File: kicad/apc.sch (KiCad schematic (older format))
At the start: 13 parts, among them U101 LM556

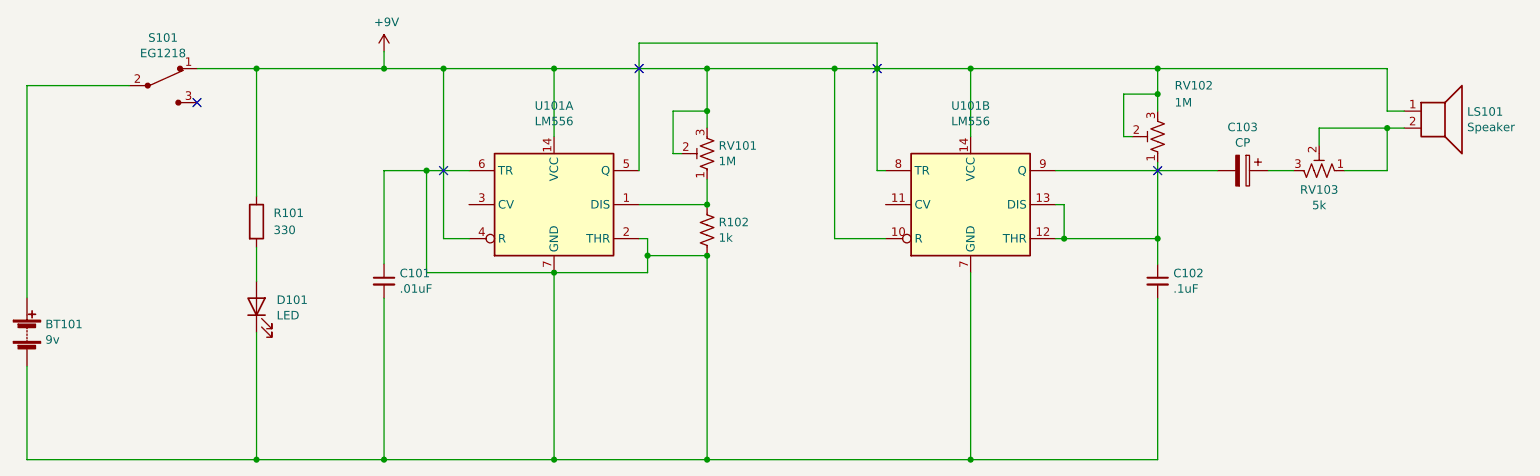
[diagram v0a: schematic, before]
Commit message: PCB revisions:
* Fix APC ground error
* Add voltage regulator to POLY_555
* Ditch hitch
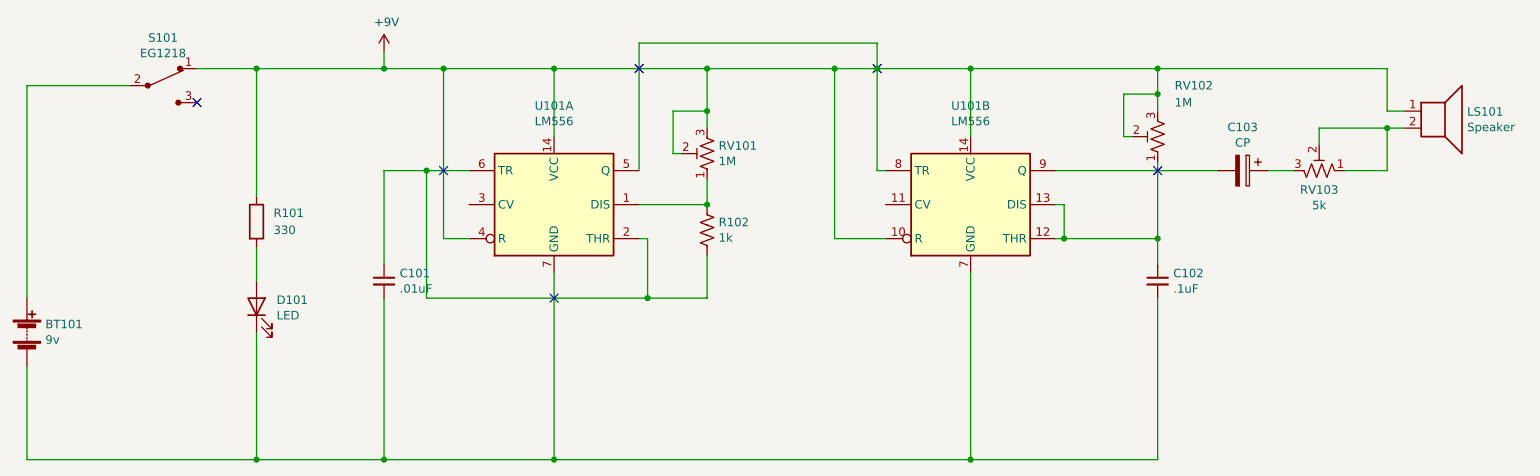
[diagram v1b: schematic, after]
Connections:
- net at BT101.2 (-), C101.2, C102.2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: no longer C101.1, R102.2, U101.2 (THR), U101.6 (TR)
- new net: C101.1, R102.2, U101.2 (THR), U101.6 (TR)
- no-connect marks 5 -> 6
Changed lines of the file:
@@
 	-1   0    0    1
-$EndComp
-$Comp
-L Timer:LM556 U101
-U 1 1 5F4726A4
-P 4150 3500
-F 0 "U101" H 4150 4081 50  0000 C CNN
-F 1 "LM556" H 4150 3990 50  0000 C CNN
-F 2 "Package_DIP:DIP-14_W7.62mm_LongPads" H 4150 3500 50  0001 C CNN
-F 3 "http://www.ti.com/lit/ds/symlink/lm556.pdf" H 4150 3500 50  0001 C CNN
-	1    4150 3500
-	1    0    0    -1
 $EndComp
 Wire Wire Line
@@
 Wire Wire Line
 	4650 3700 4700 3700
-Wire Wire Line
-	4700 3700 4700 3800
-Wire Wire Line
-	4700 3800 5050 3800
-Wire Wire Line
-	3650 3300 3400 3300
-Wire Wire Line
-	5050 5000 5050 3800
-Connection ~ 5050 3800
-Wire Wire Line
-	5050 5000 6600 5000
-Connection ~ 5050 5000
 Wire Wire Line
 	4650 3300 4650 2550
@@
 Wire Wire Line
 	3150 5000 4150 5000
-Wire Wire Line
-	4150 3900 4150 5000
 Connection ~ 4150 5000
-Wire Wire Line
-	4150 5000 5050 5000
 Wire Wire Line
 	6600 3900 6600 5000
 Connection ~ 6600 5000
-Wire Wire Line
-	3400 3300 3400 3900
-Wire Wire Line
-	3400 3900 4150 3900
-Wire Wire Line
-	4700 3900 4700 3800
-Connection ~ 3400 3300
-Wire Wire Line
-	3400 3300 3150 3300
-Connection ~ 4150 3900
-Wire Wire Line
-	4150 3900 4700 3900
-Connection ~ 4700 3800
 $Comp
 L Timer:LM556 U101
@@
 Wire Wire Line
 	6600 5000 7700 5000
+Wire Wire Line
+	4150 3900 4150 5000
+$Comp
+L Timer:LM556 U101
+U 1 1 5F4726A4
+P 4150 3500
+F 0 "U101" H 4150 4081 50  0000 C CNN
+F 1 "LM556" H 4150 3990 50  0000 C CNN
+F 2 "Package_DIP:DIP-14_W7.62mm_LongPads" H 4150 3500 50  0001 C CNN
+F 3 "http://www.ti.com/lit/ds/symlink/lm556.pdf" H 4150 3500 50  0001 C CNN
+	1    4150 3500
+	1    0    0    -1
+$EndComp
+NoConn ~ 4150 4050
+Wire Wire Line
+	4150 5000 6600 5000
+Wire Wire Line
+	5050 3800 5050 4050
+Wire Wire Line
+	5050 4050 4700 4050
+Wire Wire Line
+	3650 3300 3400 3300
+Wire Wire Line
+	3400 3300 3150 3300
+Connection ~ 3400 3300
+Wire Wire Line
+	3400 3300 3400 4050
+Connection ~ 4700 4050
+Wire Wire Line
+	4700 4050 3400 4050
+Wire Wire Line
+	4700 3700 4700 4050
 $EndSCHEMATC

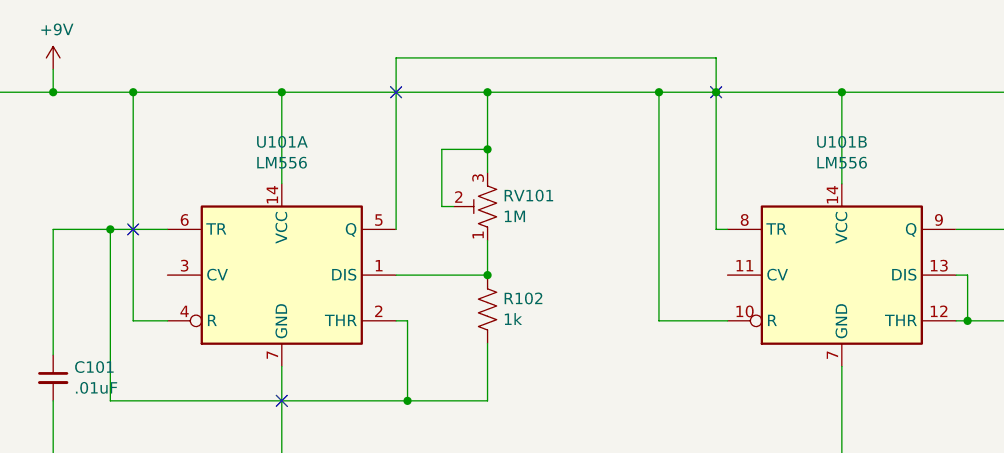
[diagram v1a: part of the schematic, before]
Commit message: Reorder components left to right
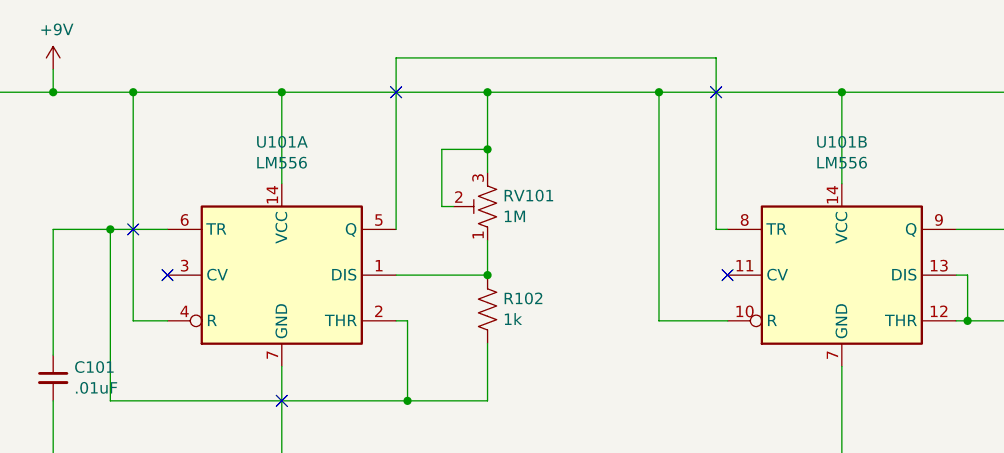
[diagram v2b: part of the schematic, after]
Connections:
- net +9V: no longer U101.5 (Q), U101.8 (TR)
- new net: U101.5 (Q), U101.8 (TR)
- no-connect marks 6 -> 8
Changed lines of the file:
@@
 	4650 3700 4700 3700
 Wire Wire Line
-	4650 3300 4650 2550
-Wire Wire Line
 	4650 2550 6050 2550
-Wire Wire Line
-	6050 2550 6050 2700
 Wire Wire Line
 	6050 3300 6100 3300
@@
 	3500 2700 4150 2700
 NoConn ~ 3500 3300
-NoConn ~ 4650 2700
-NoConn ~ 6050 2700
-Connection ~ 6050 2700
-Wire Wire Line
-	6050 2700 6600 2700
-Wire Wire Line
-	6050 2700 6050 3300
 Connection ~ 5050 2700
 $Comp
@@
 Wire Wire Line
 	7700 2700 7700 2850
-Connection ~ 6600 2700
 Wire Wire Line
 	7700 2850 7500 2850
@@
 Wire Wire Line
 	5800 3700 5800 2700
-Connection ~ 5800 2700
-Wire Wire Line
-	5800 2700 6050 2700
 Wire Wire Line
 	3150 5000 4150 5000
@@
 Wire Wire Line
 	4700 3700 4700 4050
+NoConn ~ 6100 3500
+NoConn ~ 3650 3500
+Wire Wire Line
+	5800 2700 6600 2700
+Connection ~ 5800 2700
+Connection ~ 6600 2700
+Wire Wire Line
+	4650 3300 4650 2550
+Wire Wire Line
+	6050 3300 6050 2550
+NoConn ~ 6050 2700
+NoConn ~ 4650 2700
 $EndSCHEMATC

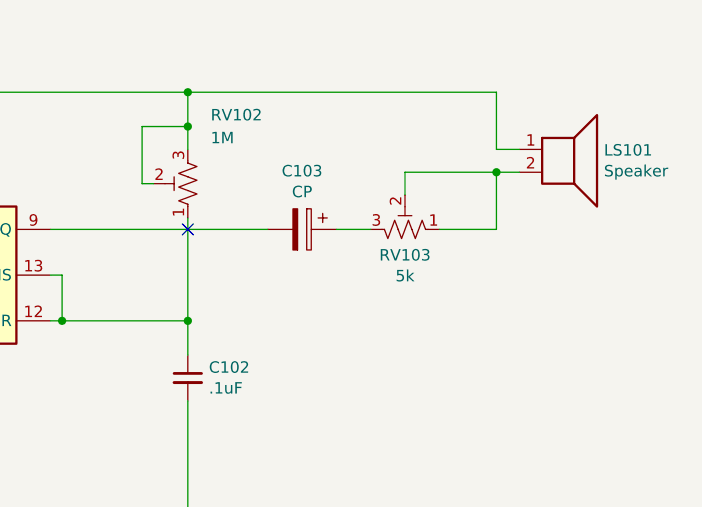
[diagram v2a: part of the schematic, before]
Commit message: APC fixes
* Reverse volume pot direction
* Reroute
* Swap timing cap footprint
* Add stress relief hole for battery wires
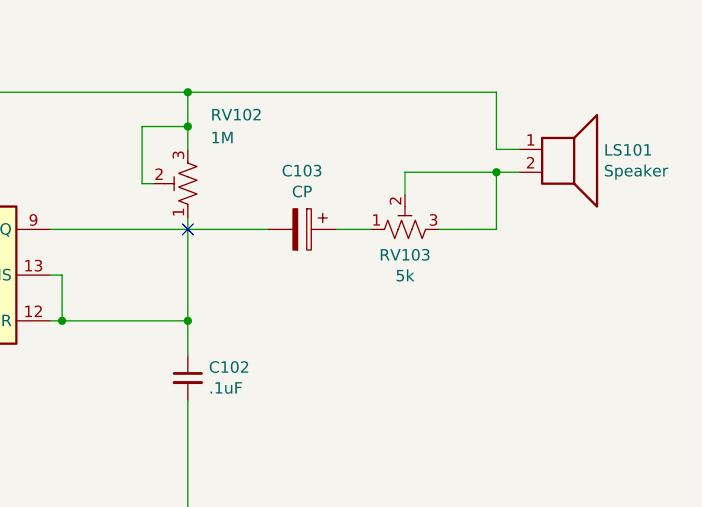
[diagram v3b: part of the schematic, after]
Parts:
- C103: footprint Capacitor_THT:CP_Radial_D8.0mm_P3.50mm -> Capacitor_THT:CP_Radial_D4.0mm_P2.00mm
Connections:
- net at LS101.2, RV103.2: now also RV103.3; no longer RV103.1
- net at C103.1: now also RV103.1; no longer RV103.3
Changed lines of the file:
@@
 	7700 3700 7700 3850
 Connection ~ 7150 3700
-$Comp
-L Device:R_POT_TRIM_US RV102
-U 1 1 5F48C811
-P 7700 3100
-F 0 "RV102" H 7600 2800 50  0000 R CNN
-F 1 "1M" H 7600 2900 50  0000 R CNN
-F 2 "Potentiometer_THT:Potentiometer_Piher_PT-6-V_Vertical" H 7700 3100 50  0001 C CNN
-F 3 "~" H 7700 3100 50  0001 C CNN
-	1    7700 3100
-	-1   0    0    1
-$EndComp
-Wire Wire Line
-	7550 3100 7500 3100
-Wire Wire Line
-	7500 3100 7500 2850
 Wire Wire Line
 	6600 2700 7700 2700
-Wire Wire Line
-	7700 2700 7700 2850
-Wire Wire Line
-	7700 2850 7500 2850
-Connection ~ 7700 2850
-Wire Wire Line
-	7700 2850 7700 2950
 Wire Wire Line
 	7700 3250 7700 3700
@@
 	1    0    0    -1
 $EndComp
-$Comp
-L Device:CP C103
-U 1 1 5F496041
-P 8200 3300
-F 0 "C103" V 7945 3300 50  0000 C CNN
-F 1 "CP" V 8036 3300 50  0000 C CNN
-F 2 "Capacitor_THT:CP_Radial_D8.0mm_P3.50mm" H 8238 3150 50  0001 C CNN
-F 3 "~" H 8200 3300 50  0001 C CNN
-	1    8200 3300
-	0    1    1    0
-$EndComp
 Wire Wire Line
 	7700 2700 9050 2700
@@
 	8050 3300 7100 3300
 NoConn ~ 7700 3300
-$Comp
-L Device:R_POT_TRIM_US RV103
-U 1 1 5F4918D3
-P 8650 3300
-F 0 "RV103" V 8537 3300 50  0000 C CNN
-F 1 "5k" V 8446 3300 50  0000 C CNN
-F 2 "Potentiometer_THT:Potentiometer_Piher_PT-6-V_Vertical" H 8650 3300 50  0001 C CNN
-F 3 "~" H 8650 3300 50  0001 C CNN
-	1    8650 3300
-	0    1    -1   0
-$EndComp
-Wire Wire Line
-	9050 3050 8650 3050
-Wire Wire Line
-	8650 3050 8650 3150
-Connection ~ 9050 3050
-Wire Wire Line
-	8350 3300 8500 3300
-Wire Wire Line
-	8800 3300 9050 3300
 Wire Wire Line
 	5800 3700 5800 2700
@@
 	6050 3300 6050 2550
 NoConn ~ 6050 2700
+Wire Wire Line
+	7550 3100 7500 3100
+$Comp
+L Device:R_POT_TRIM_US RV102
+U 1 1 5F48C811
+P 7700 3100
+F 0 "RV102" H 7600 2800 50  0000 R CNN
+F 1 "1M" H 7600 2900 50  0000 R CNN
+F 2 "Potentiometer_THT:Potentiometer_Piher_PT-6-V_Vertical" H 7700 3100 50  0001 C CNN
+F 3 "~" H 7700 3100 50  0001 C CNN
+	1    7700 3100
+	-1   0    0    1
+$EndComp
+Wire Wire Line
+	7500 3100 7500 2850
 NoConn ~ 4650 2700
+Wire Wire Line
+	7700 2850 7700 2950
+Wire Wire Line
+	7700 2700 7700 2850
+Connection ~ 7700 2850
+Wire Wire Line
+	7700 2850 7500 2850
+$Comp
+L Device:CP C103
+U 1 1 5F496041
+P 8200 3300
+F 0 "C103" V 7945 3300 50  0000 C CNN
+F 1 "CP" V 8036 3300 50  0000 C CNN
+F 2 "Capacitor_THT:CP_Radial_D4.0mm_P2.00mm" H 8238 3150 50  0001 C CNN
+F 3 "~" H 8200 3300 50  0001 C CNN
+	1    8200 3300
+	0    1    1    0
+$EndComp
+$Comp
+L Device:R_POT_TRIM_US RV103
+U 1 1 5F4918D3
+P 8650 3300
+F 0 "RV103" V 8537 3300 50  0000 C CNN
+F 1 "5k" V 8446 3300 50  0000 C CNN
+F 2 "Potentiometer_THT:Potentiometer_Piher_PT-6-V_Vertical" H 8650 3300 50  0001 C CNN
+F 3 "~" H 8650 3300 50  0001 C CNN
+	1    8650 3300
+	0    -1   -1   0
+$EndComp
+Wire Wire Line
+	8350 3300 8500 3300
+Wire Wire Line
+	8800 3300 9050 3300
+Wire Wire Line
+	9050 3050 8650 3050
+Wire Wire Line
+	8650 3050 8650 3150
+Connection ~ 9050 3050
 $EndSCHEMATC

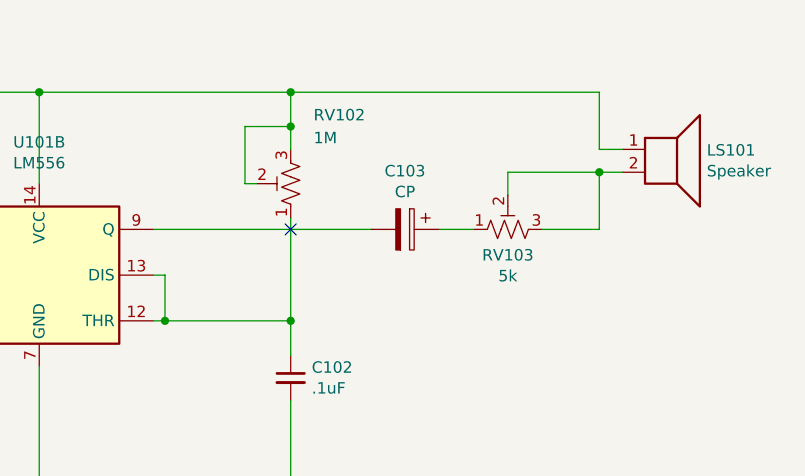
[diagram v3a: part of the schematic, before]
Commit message: Update PCB
* Fix and expand battery cavity
* Fix S13-S20,C61,U21 label placements
* Fix uneven breakaway wall near APC
* Swap misplaced C62,R83 labels
* Assign C103 value
* Swap 4.7uF cap footprints and re-route
* Move LED
* Upgrade APC pots
* Move to 0,0
* Expand battery cavity even more
* Update branding: ditch _ and space, add rev, add to back side too
* Add APC rev too
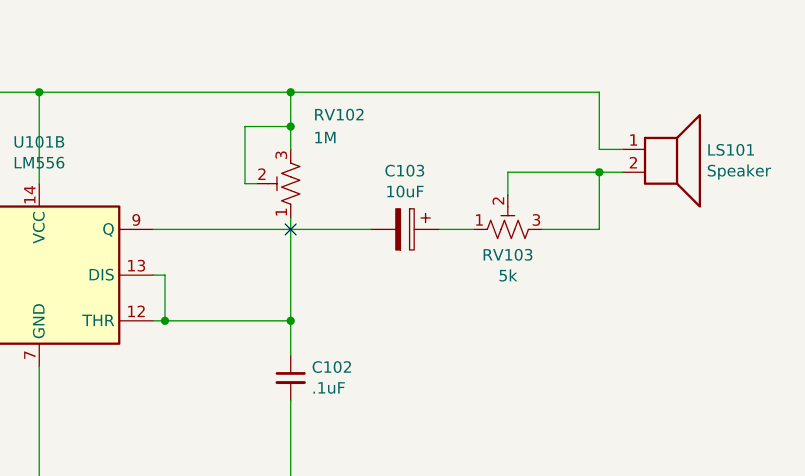
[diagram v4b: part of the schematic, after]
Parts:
- C103: value CP -> 10uF
- RV101, RV102: footprint Potentiometer_THT:Potentiometer_Piher_PT-6-V_Vertical -> Potentiometer_THT:Potentiometer_Bourns_PTV09A-2_Single_Horizontal
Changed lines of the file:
@@
 F 0 "RV101" H 4982 3154 50  0000 R CNN
 F 1 "1M" H 4982 3245 50  0000 R CNN
-F 2 "Potentiometer_THT:Potentiometer_Piher_PT-6-V_Vertical" H 5050 3200 50  0001 C CNN
+F 2 "Potentiometer_THT:Potentiometer_Bourns_PTV09A-2_Single_Horizontal" H 5050 3200 50  0001 C CNN
 F 3 "~" H 5050 3200 50  0001 C CNN
 	1    5050 3200
@@
 F 0 "RV102" H 7600 2800 50  0000 R CNN
 F 1 "1M" H 7600 2900 50  0000 R CNN
-F 2 "Potentiometer_THT:Potentiometer_Piher_PT-6-V_Vertical" H 7700 3100 50  0001 C CNN
+F 2 "Potentiometer_THT:Potentiometer_Bourns_PTV09A-2_Single_Horizontal" H 7700 3100 50  0001 C CNN
 F 3 "~" H 7700 3100 50  0001 C CNN
 	1    7700 3100
@@
 P 8200 3300
 F 0 "C103" V 7945 3300 50  0000 C CNN
-F 1 "CP" V 8036 3300 50  0000 C CNN
+F 1 "10uF" V 8036 3300 50  0000 C CNN
 F 2 "Capacitor_THT:CP_Radial_D4.0mm_P2.00mm" H 8238 3150 50  0001 C CNN
 F 3 "~" H 8200 3300 50  0001 C CNN
